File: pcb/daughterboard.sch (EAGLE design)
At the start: 21 parts, among them IC3 STM32F042F4, SW1 324_SW324_SWITCH_FOOT_HOLE, SW2 324_SW324_SWITCH_FOOT_HOLE, SW3 324_SW, SW4 324_SW, SW5 324_SW324_SWITCH_FOOT_HOLE, SW6 324_SW324_SWITCH_FOOT_HOLE, U2 USBC_16P, U4 XC6206_DEV

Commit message: working on new version
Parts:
- C4: value 1uF -> 100nF
- JP1: device pinhead:PINHD-2X4 -> pinhead:PINHD-2X3
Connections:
- new net N$1: IC3.PB1, JP1.4
- net +3V3: no longer LED2.A
- net +5V: now also JP1.1
- net GND: now also JP1.2
- net USB_DN: now also IC3.PA9/PA11
- net USB_DP: now also IC3.PA10/PA12
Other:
- moved on the sheet: JP3, LED2, R6
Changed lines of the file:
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@@
 <part name="+3V1" library="supply1" library_urn="urn:adsk.eagle:library:371" deviceset="+3V3" device=""/>
 <part name="GND5" library="supply1" deviceset="GND" device=""/>
-<part name="C4" library="clock" deviceset="CAP" device="0805" value="1uF"/>
+<part name="C4" library="clock" deviceset="CAP" device="0805" value="100nF"/>
 <part name="GND8" library="supply1" deviceset="GND" device=""/>
 <part name="GND11" library="supply1" library_urn="urn:adsk.eagle:library:371" deviceset="GND" device=""/>
 <part name="SW3" library="3pos_slide_switch_centered" deviceset="324_SW" device="" value="324_SW"/>
 <part name="SW4" library="3pos_slide_switch_centered" deviceset="324_SW" device="" value="324_SW"/>
-<part name="+3V16" library="backplane" deviceset="+3V3" device=""/>
 <part name="LED2" library="adafruit" deviceset="LED" device="CHIP-LED0805"/>
 <part name="R6" library="SparkFun-Passives" deviceset="RESISTOR" device="0805-RES" value="1K"/>
@@
 <part name="U4" library="3pos_slide_switch" deviceset="XC6206_DEV" device=""/>
 <part name="C2" library="clock" deviceset="CAP" device="0805" value="1uF"/>
-<part name="JP1" library="pinhead" library_urn="urn:adsk.eagle:library:325" deviceset="PINHD-2X4" device="" package3d_urn="urn:adsk.eagle:package:22461/2"/>
+<part name="JP1" library="pinhead" library_urn="urn:adsk.eagle:library:325" deviceset="PINHD-2X3" device="" package3d_urn="urn:adsk.eagle:package:22462/2"/>
 <part name="SW2" library="3pos_slide_switch" deviceset="324_SW" device="324_SWITCH_FOOT_HOLE" value="324_SW324_SWITCH_FOOT_HOLE"/>
 <part name="SW1" library="3pos_slide_switch" deviceset="324_SW" device="324_SWITCH_FOOT_HOLE" value="324_SW324_SWITCH_FOOT_HOLE"/>
@@
 <part name="JP3" library="pinhead" library_urn="urn:adsk.eagle:library:325" deviceset="PINHD-1X3" device="" package3d_urn="urn:adsk.eagle:package:22458/2"/>
 <part name="JP4" library="pinhead" library_urn="urn:adsk.eagle:library:325" deviceset="PINHD-1X2" device="" package3d_urn="urn:adsk.eagle:package:22435/2"/>
+<part name="P+2" library="supply1" library_urn="urn:adsk.eagle:library:371" deviceset="+5V" device=""/>
+<part name="GND2" library="supply1" deviceset="GND" device=""/>
 </parts>
 <sheets>
@@
 <instance part="SW3" gate="G$1" x="91.44" y="55.88" smashed="yes" rot="R90"/>
 <instance part="SW4" gate="G$1" x="91.44" y="2.54" smashed="yes" rot="MR270"/>
-<instance part="+3V16" gate="G$1" x="106.68" y="73.66" smashed="yes" rot="MR0">
-<attribute name="VALUE" x="109.22" y="68.58" size="1.778" layer="96" rot="MR90"/>
-</instance>
-<instance part="LED2" gate="G$1" x="109.22" y="71.12" smashed="yes" rot="R90">
-<attribute name="NAME" x="113.792" y="74.676" size="1.778" layer="95" rot="R180"/>
-<attribute name="VALUE" x="113.792" y="76.835" size="1.778" layer="96" rot="R180"/>
-</instance>
-<instance part="R6" gate="G$1" x="119.38" y="71.12" smashed="yes" rot="R180">
-<attribute name="NAME" x="123.19" y="69.6214" size="1.778" layer="95" rot="R180"/>
-<attribute name="VALUE" x="123.19" y="74.422" size="1.778" layer="96" rot="R180"/>
-</instance>
-<instance part="GND9" gate="1" x="124.46" y="68.58" smashed="yes">
-<attribute name="VALUE" x="121.92" y="66.04" size="1.778" layer="96"/>
+<instance part="LED2" gate="G$1" x="134.62" y="25.4" smashed="yes" rot="R90">
+<attribute name="NAME" x="139.192" y="28.956" size="1.778" layer="95" rot="R180"/>
+<attribute name="VALUE" x="139.192" y="31.115" size="1.778" layer="96" rot="R180"/>
+</instance>
+<instance part="R6" gate="G$1" x="144.78" y="25.4" smashed="yes" rot="R180">
+<attribute name="NAME" x="148.59" y="23.9014" size="1.778" layer="95" rot="R180"/>
+<attribute name="VALUE" x="148.59" y="28.702" size="1.778" layer="96" rot="R180"/>
+</instance>
+<instance part="GND9" gate="1" x="149.86" y="22.86" smashed="yes">
+<attribute name="VALUE" x="147.32" y="20.32" size="1.778" layer="96"/>
 </instance>
 <instance part="+3V2" gate="G$1" x="93.98" y="25.4" smashed="yes" rot="MR0">
@@
 <attribute name="VALUE" x="143.256" y="118.999" size="1.778" layer="96" rot="R180"/>
 </instance>
-<instance part="JP1" gate="A" x="-55.88" y="71.12" smashed="yes">
-<attribute name="NAME" x="-62.23" y="76.835" size="1.778" layer="95"/>
-<attribute name="VALUE" x="-62.23" y="63.5" size="1.778" layer="96"/>
+<instance part="JP1" gate="A" x="2.54" y="73.66" smashed="yes">
+<attribute name="NAME" x="-3.81" y="79.375" size="1.778" layer="95"/>
+<attribute name="VALUE" x="-3.81" y="66.04" size="1.778" layer="96"/>
 </instance>
 <instance part="SW2" gate="G$1" x="-60.96" y="106.68" smashed="yes" rot="MR90"/>
@@
 <attribute name="VALUE" x="-90.17" y="15.24" size="1.778" layer="96"/>
 </instance>
-<instance part="JP3" gate="A" x="-35.56" y="50.8" smashed="yes">
-<attribute name="NAME" x="-41.91" y="56.515" size="1.778" layer="95"/>
-<attribute name="VALUE" x="-41.91" y="43.18" size="1.778" layer="96"/>
+<instance part="JP3" gate="A" x="-50.8" y="58.42" smashed="yes">
+<attribute name="NAME" x="-57.15" y="64.135" size="1.778" layer="95"/>
+<attribute name="VALUE" x="-57.15" y="50.8" size="1.778" layer="96"/>
 </instance>
 <instance part="JP4" gate="G$1" x="-53.34" y="33.02" smashed="yes">
 <attribute name="NAME" x="-59.69" y="38.735" size="1.778" layer="95"/>
 <attribute name="VALUE" x="-59.69" y="27.94" size="1.778" layer="96"/>
+</instance>
+<instance part="P+2" gate="1" x="-12.7" y="81.28" smashed="yes">
+<attribute name="VALUE" x="-15.24" y="76.2" size="1.778" layer="96" rot="R90"/>
+</instance>
+<instance part="GND2" gate="1" x="27.94" y="73.66" smashed="yes" rot="MR0">
+<attribute name="VALUE" x="30.48" y="71.12" size="1.778" layer="96" rot="MR0"/>
 </instance>
 </instances>
@@
 <wire x1="144.78" y1="111.76" x2="144.78" y2="109.22" width="0.1524" layer="91"/>
 </segment>
+<segment>
+<pinref part="JP1" gate="A" pin="2"/>
+<pinref part="GND2" gate="1" pin="GND"/>
+<wire x1="7.62" y1="76.2" x2="27.94" y2="76.2" width="0.1524" layer="91"/>
+</segment>
 </net>
 <net name="+3V3" class="0">
@@
 </segment>
 <segment>
-<pinref part="+3V16" gate="G$1" pin="+3V3"/>
-<pinref part="LED2" gate="G$1" pin="A"/>
-</segment>
-<segment>
 <pinref part="SW4" gate="G$1" pin="1"/>
 <pinref part="SW4" gate="G$1" pin="4"/>
@@
 <wire x1="40.64" y1="114.3" x2="38.1" y2="114.3" width="0.1524" layer="91"/>
 </segment>
+<segment>
+<pinref part="IC3" gate="G$1" pin="PA10/PA12"/>
+<wire x1="-17.78" y1="17.78" x2="-30.48" y2="17.78" width="0.1524" layer="91"/>
+<label x="-30.48" y="17.78" size="1.778" layer="95"/>
+</segment>
 </net>
 <net name="N$31" class="0">
@@
 <wire x1="40.64" y1="106.68" x2="40.64" y2="109.22" width="0.1524" layer="91"/>
 <junction x="40.64" y="109.22"/>
+</segment>
+<segment>
+<pinref part="IC3" gate="G$1" pin="PA9/PA11"/>
+<wire x1="-17.78" y1="20.32" x2="-30.48" y2="20.32" width="0.1524" layer="91"/>
+<label x="-30.48" y="20.32" size="1.778" layer="95"/>
 </segment>
 </net>
@@
 <junction x="60.96" y="121.92"/>
 <pinref part="U4" gate="G$1" pin="IN"/>
+</segment>
+<segment>
+<pinref part="JP1" gate="A" pin="1"/>
+<pinref part="P+2" gate="1" pin="+5V"/>
+<wire x1="0" y1="76.2" x2="-12.7" y2="76.2" width="0.1524" layer="91"/>
+<wire x1="-12.7" y1="76.2" x2="-12.7" y2="78.74" width="0.1524" layer="91"/>
 </segment>
 </net>
@@
 </segment>
 </net>
+<net name="N$1" class="0">
+<segment>
+<pinref part="IC3" gate="G$1" pin="PB1"/>
+<wire x1="-17.78" y1="7.62" x2="-35.56" y2="7.62" width="0.1524" layer="91"/>
+<wire x1="-35.56" y1="7.62" x2="-35.56" y2="60.96" width="0.1524" layer="91"/>
+<wire x1="-35.56" y1="60.96" x2="17.78" y2="60.96" width="0.1524" layer="91"/>
+<wire x1="17.78" y1="60.96" x2="17.78" y2="73.66" width="0.1524" layer="91"/>
+<pinref part="JP1" gate="A" pin="4"/>
+<wire x1="17.78" y1="73.66" x2="7.62" y2="73.66" width="0.1524" layer="91"/>
+</segment>
+</net>

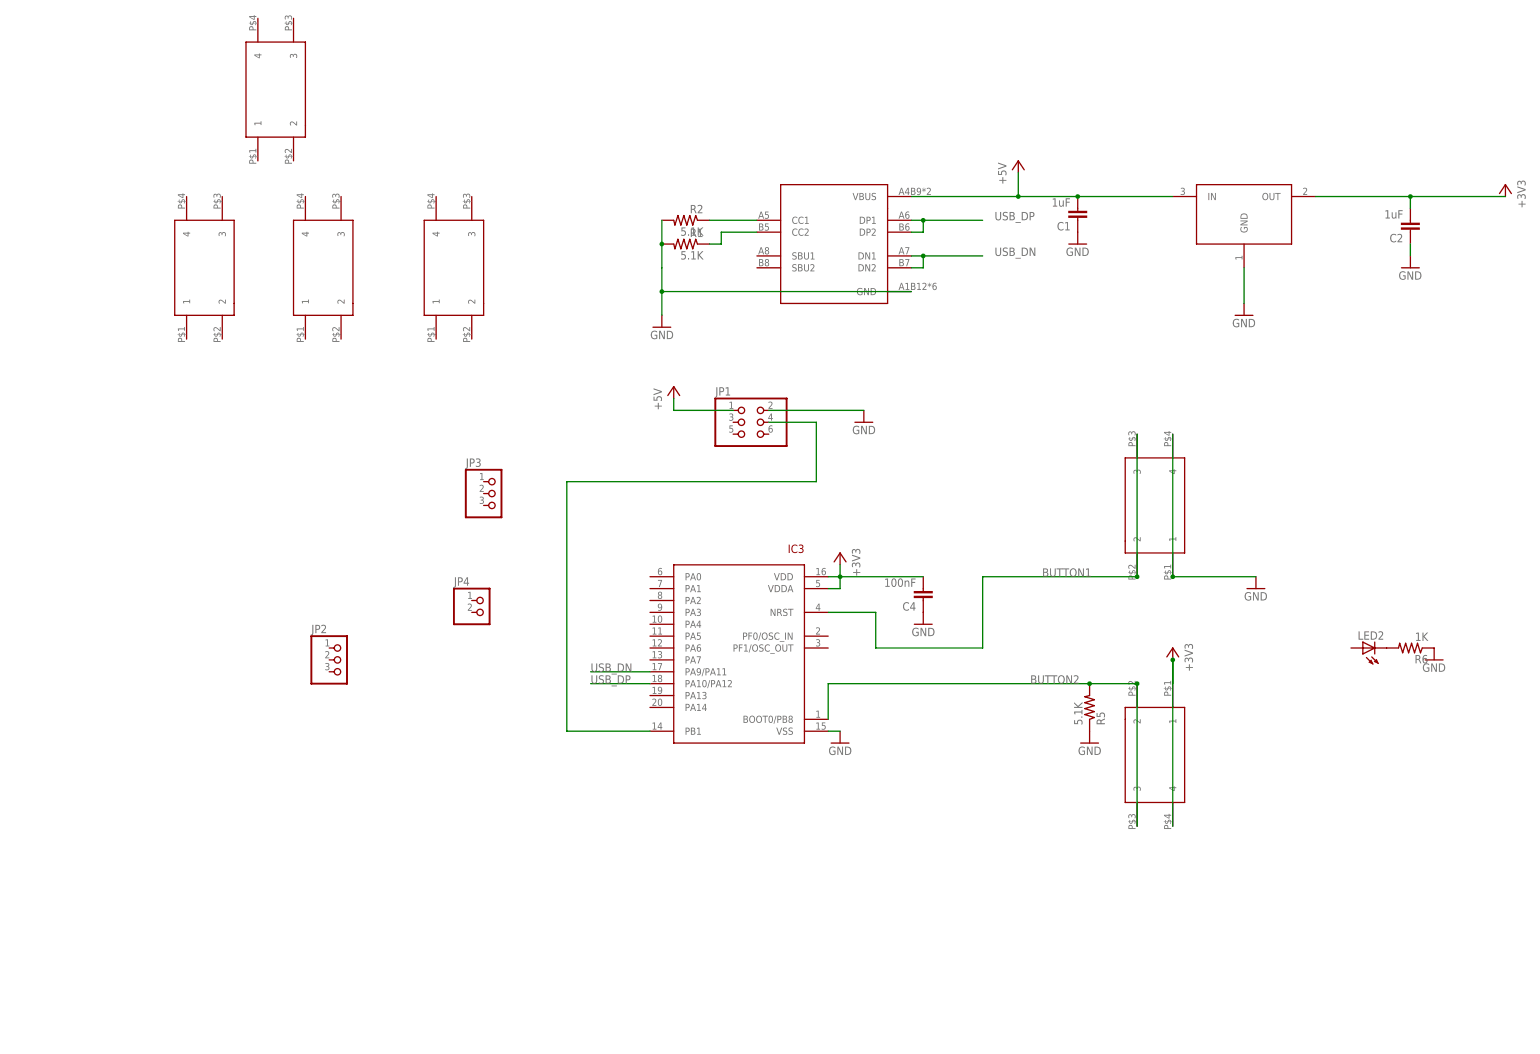
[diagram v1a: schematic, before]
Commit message: new daughterboard
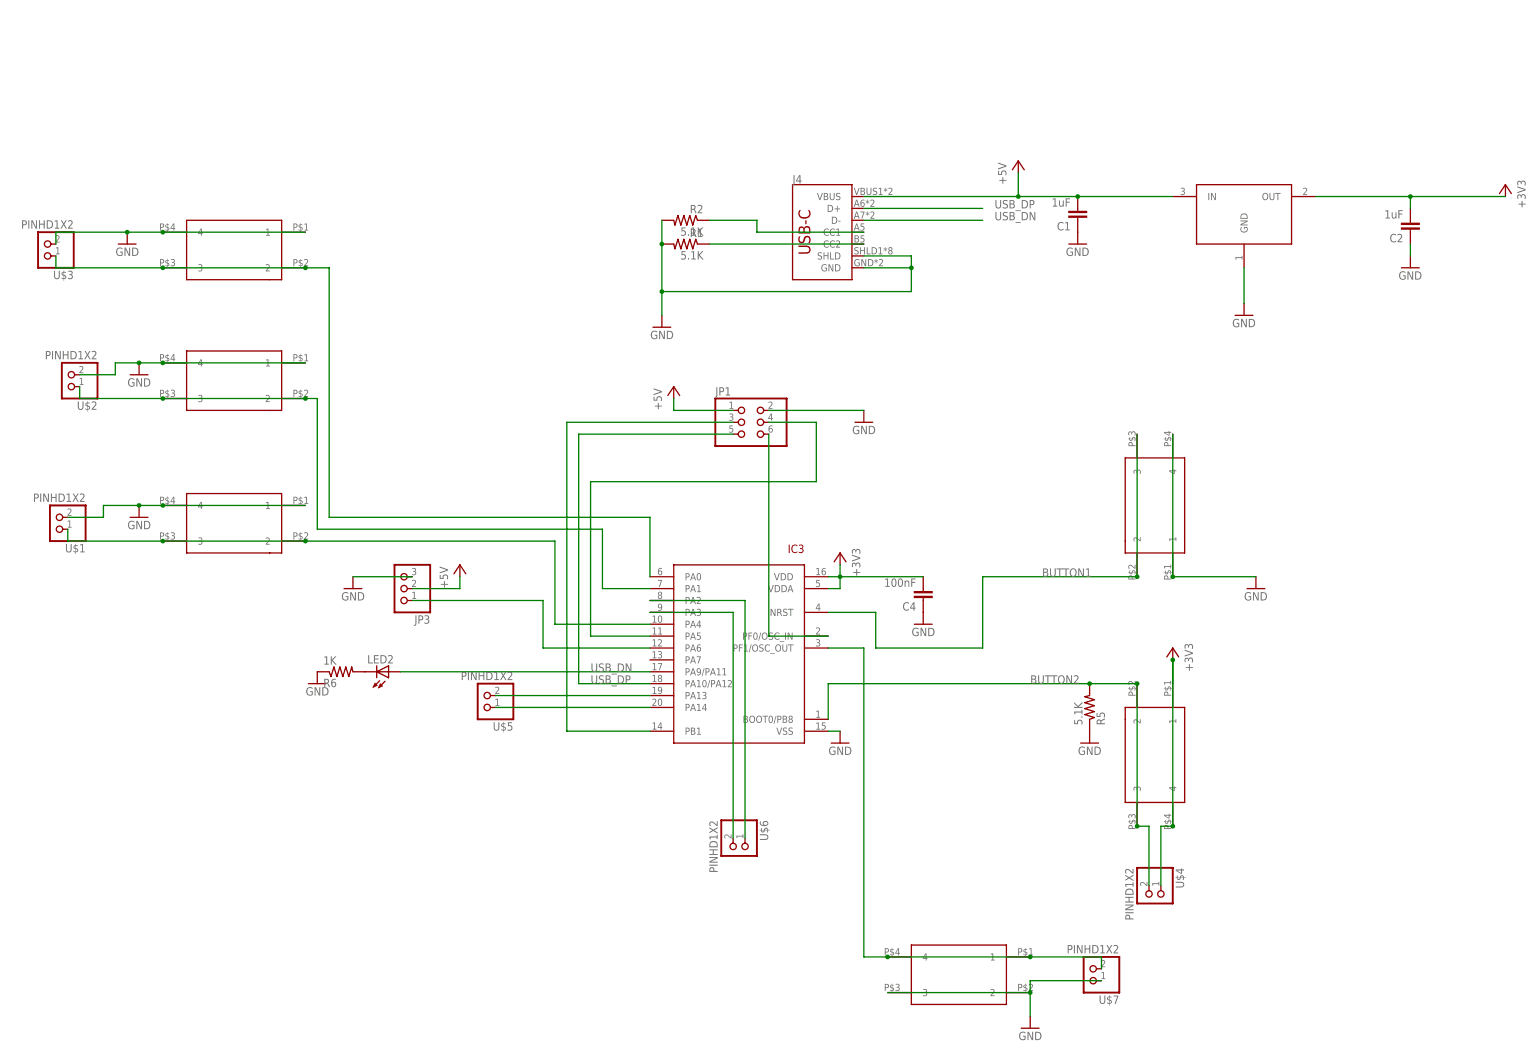
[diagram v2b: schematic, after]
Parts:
- removed JP2: (no value), pinhead:PINHD-1X3
- removed JP4: (no value), pinhead:PINHD-1X2
- removed U2: USBC_16P, my_usbc_16p:USBC_16P
- added J4: (no value), SparkFun-Connectors:USB_C16PIN
- added U$1, U$2, U$3, U$4, U$5, U$6, U$7: PINHD1X2, adafruit_changed:PINHD1X2
- JP3: device pinhead:PINHD-1X3 -> adafruit_changed:PINHD-1X3CB
- SW1, SW2, SW5, SW6: value 324_SW324_SWITCH_FOOT_HOLE -> 324_SW; device 3pos_slide_switch:324_SW324_SWITCH_FOOT_HOLE -> 3pos_slide_switch_centered:324_SW
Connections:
- new net N$10: IC3.PA1, SW2.2, SW2.3, U$2.1
- new net N$11: IC3.PA0, SW5.2, SW5.3, U$3.1
- new net N$12: IC3.PF1/OSC_OUT, SW6.1, SW6.4, U$7.2
- new net N$2: IC3.PB1, JP1.3
- new net N$3: IC3.PA13, U$5.2
- new net N$4: IC3.PA14, U$5.1
- new net N$5: IC3.PA6, JP3.1
- new net N$6: IC3.PF0/OSC_IN, JP1.6
- new net N$7: IC3.PA2, U$6.1
- new net N$8: IC3.PA3, U$6.2
- new net N$9: IC3.PA4, SW1.2, SW1.3, U$1.1
- net +3V3: now also U$4.1
- net +5V: now also J4.VBUS, JP3.2; no longer U2.VBUS
- net BUTTON2: now also U$4.2
- net GND: now also J4.GND, J4.SHLD, JP3.3, SW1.1, SW1.4, SW2.1, SW2.4, SW5.1, SW5.4, SW6.2, SW6.3, U$1.2, U$2.2, U$3.2, U$7.1; no longer U2.GND
- net N$1: now also IC3.PA5; no longer IC3.PB1
- net N$31: now also J4.CC2; no longer U2.CC2
- net N$33: now also J4.CC1; no longer U2.CC1
- net USB_DN: now also J4.D-, LED2.A; no longer U2.DN1, U2.DN2
- net USB_DP: now also J4.D+, JP1.5; no longer U2.DP1, U2.DP2
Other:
- moved on the sheet: JP3, LED2, R6

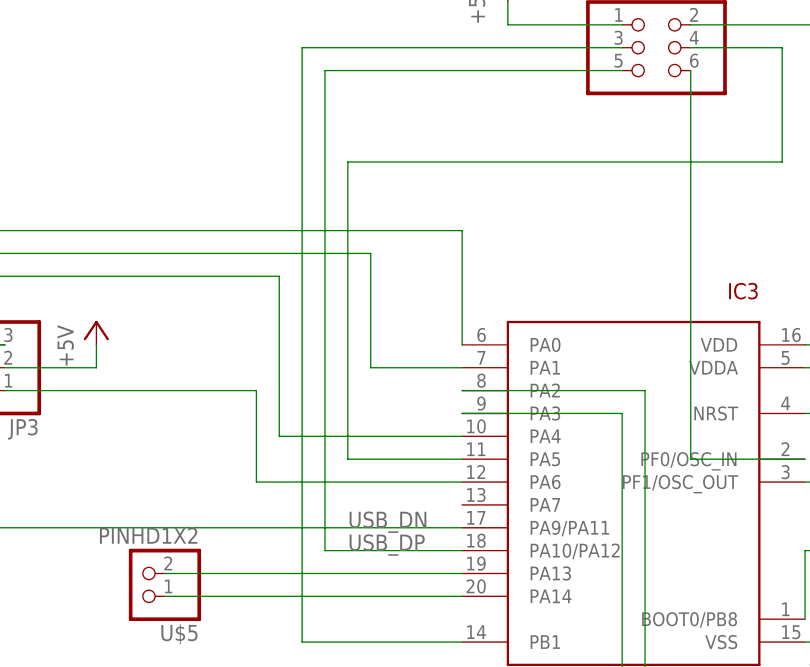
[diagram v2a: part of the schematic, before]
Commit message: fixed a wrong signal
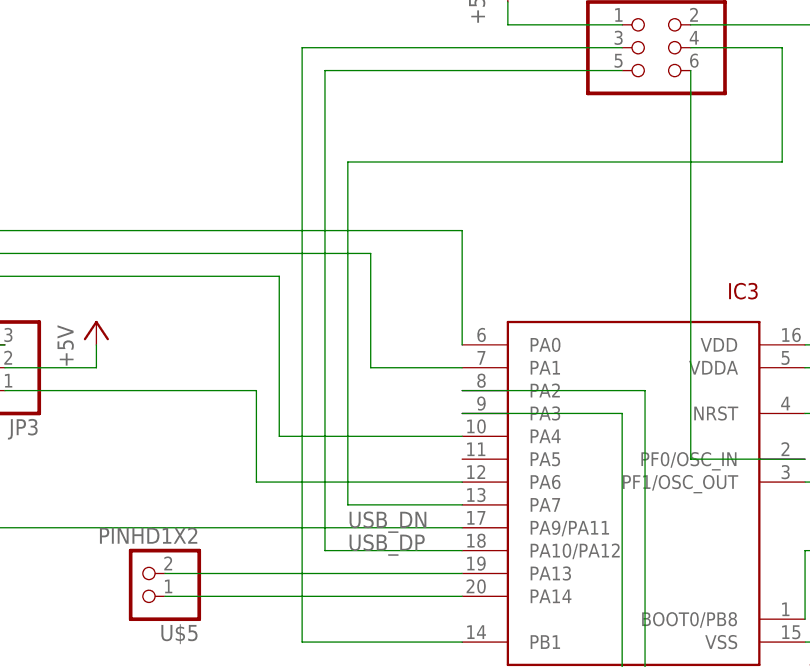
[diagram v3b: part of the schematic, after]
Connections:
- net N$1: now also IC3.PA7; no longer IC3.PA5
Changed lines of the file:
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@@
 <wire x1="17.78" y1="73.66" x2="7.62" y2="73.66" width="0.1524" layer="91"/>
 <wire x1="17.78" y1="60.96" x2="-30.48" y2="60.96" width="0.1524" layer="91"/>
-<wire x1="-30.48" y1="60.96" x2="-30.48" y2="27.94" width="0.1524" layer="91"/>
-<pinref part="IC3" gate="G$1" pin="PA5"/>
-<wire x1="-30.48" y1="27.94" x2="-17.78" y2="27.94" width="0.1524" layer="91"/>
+<wire x1="-30.48" y1="60.96" x2="-30.48" y2="22.86" width="0.1524" layer="91"/>
+<pinref part="IC3" gate="G$1" pin="PA7"/>
+<wire x1="-17.78" y1="22.86" x2="-30.48" y2="22.86" width="0.1524" layer="91"/>
 </segment>
 </net>
